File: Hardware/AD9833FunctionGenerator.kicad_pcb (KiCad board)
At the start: 4 copper layers, 50.8 x 128.3 mm, 37 parts, among them U1 LM7805_TO220

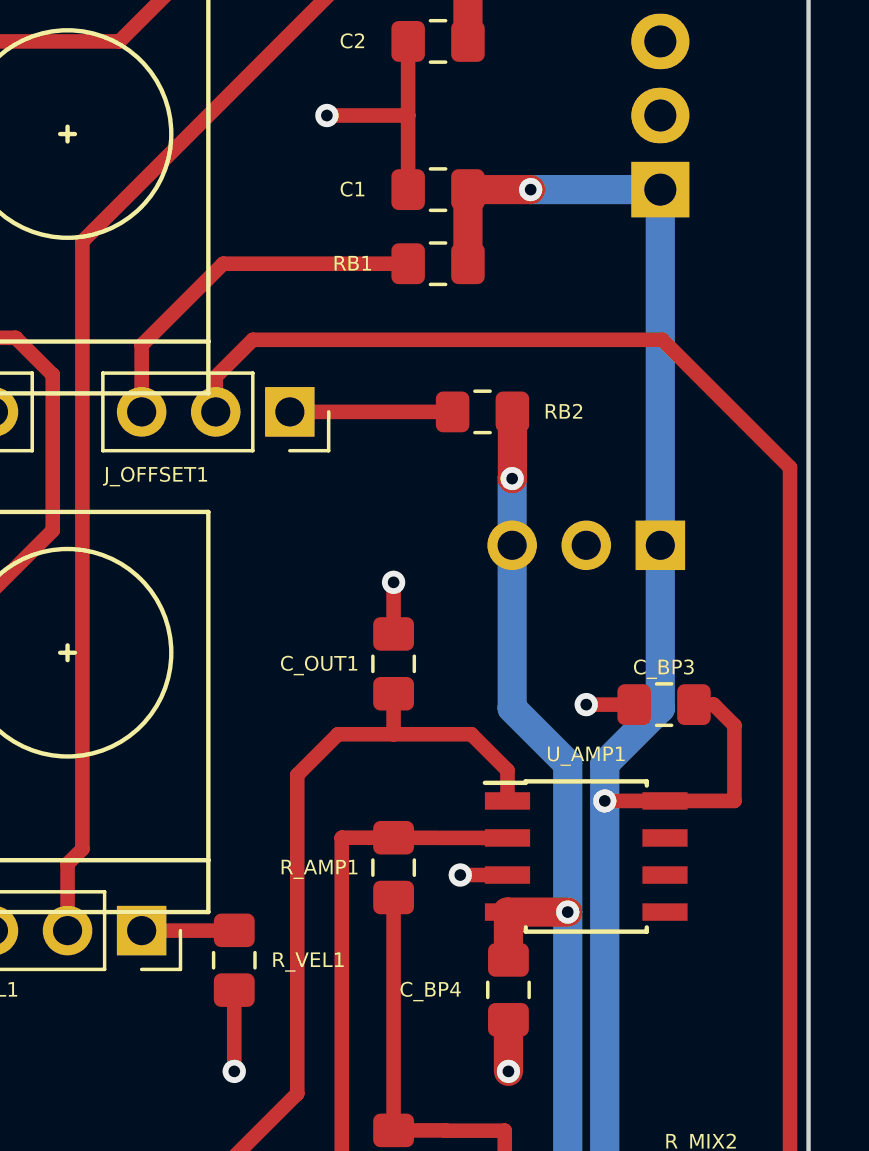
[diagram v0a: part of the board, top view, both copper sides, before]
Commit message: Changed J_PWR1 from 01x03 to 02x05
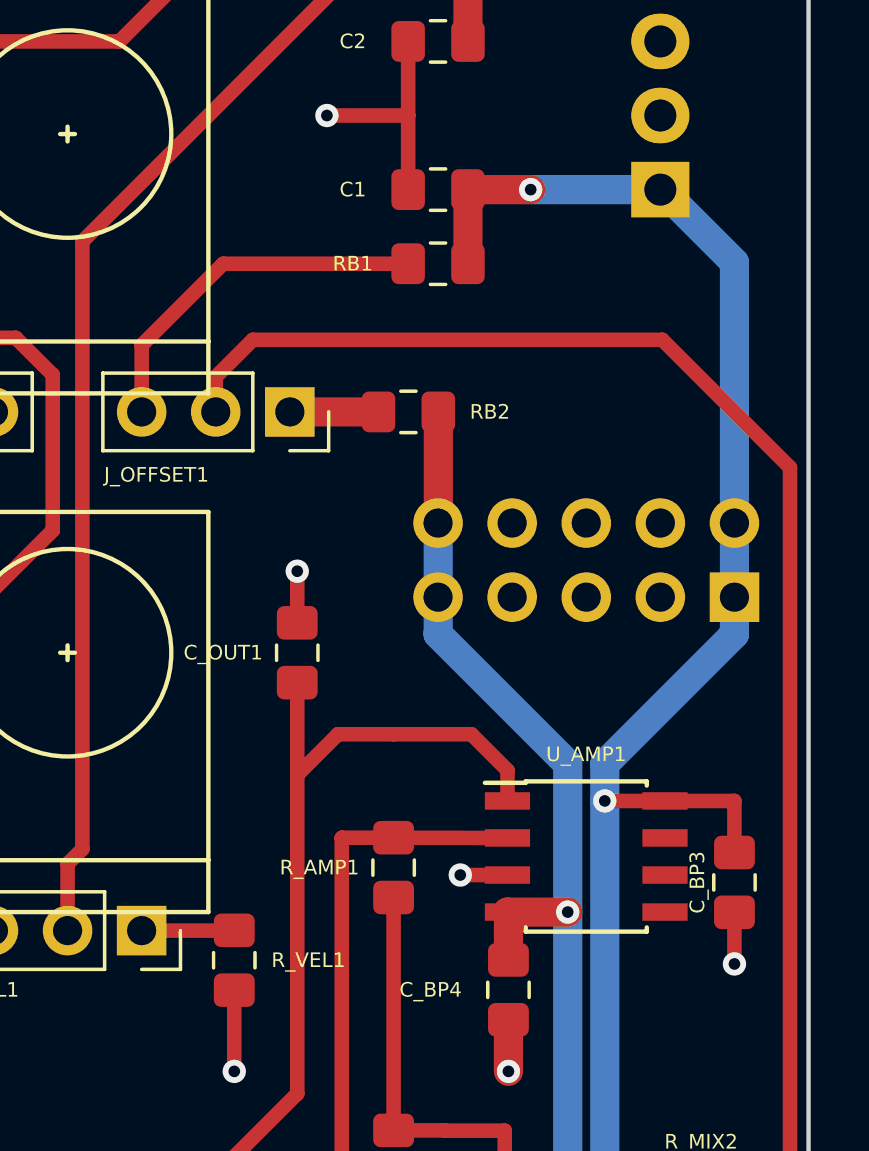
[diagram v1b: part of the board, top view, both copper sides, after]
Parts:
- J_PWR1: value Conn_01x03 -> Conn_02x05_Odd_Even; footprint Connector_PinSocket_2.54mm:PinSocket_1x03_P2.54mm_Vertical -> Connector_PinHeader_2.54mm:PinHeader_2x05_P2.54mm_Vertical
- moved C_BP3 6.56 mm to (99.1, 120.3), turned to 270 degrees
- moved C_OUT1 3.32 mm to (84.1, 112.4)
- moved J_PWR1 3.10 mm to (99.1, 110.5)
- moved RB2 2.54 mm to (87.9, 104.1)
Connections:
- J_PWR1 pad 2: /GND -> /+12V
- J_PWR1 pad 3: /-12V -> /GND
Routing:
- net Net-(J_OFFSET1-Pad1): track 5.58 -> 3.04 mm
- net Net-(C_OUT1-Pad1): track 145.1 -> 146.8 mm
- net /-12V: track 49.8 -> 50.8 mm, vias 3 -> 2
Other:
- board text added: "+12V"
- board text added: "-12V"
- board text added: "| —-— GND —-— |"

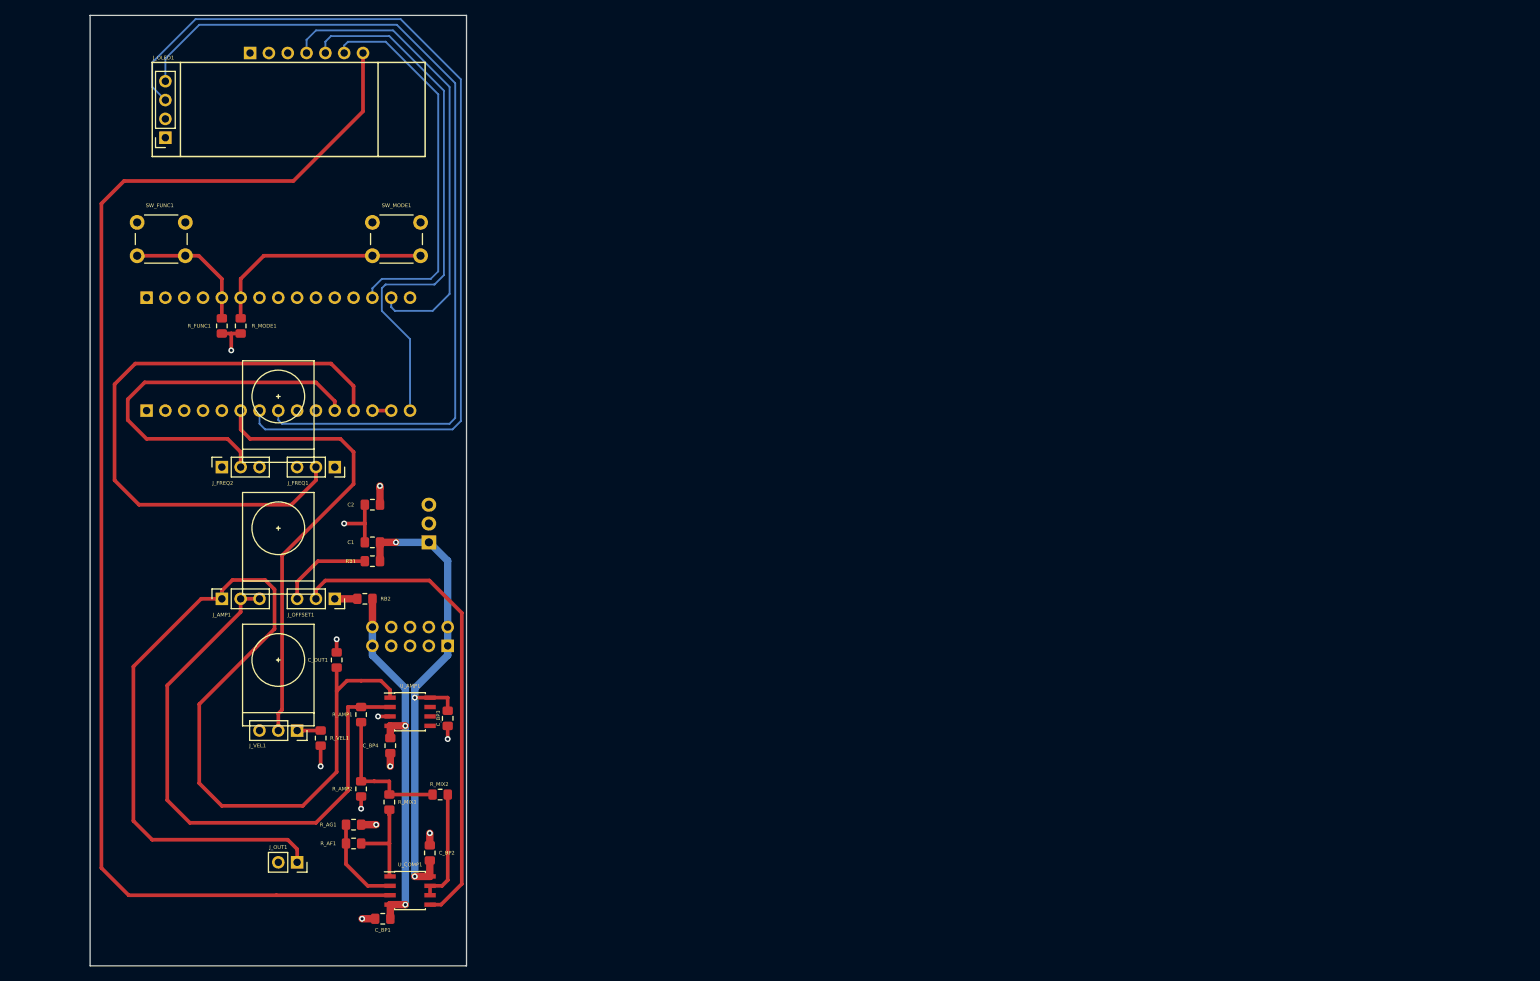
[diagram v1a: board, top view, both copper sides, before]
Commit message: Created board layout RevB. Right-angled to front panel, with front facing aux board(OLED/Buttons)
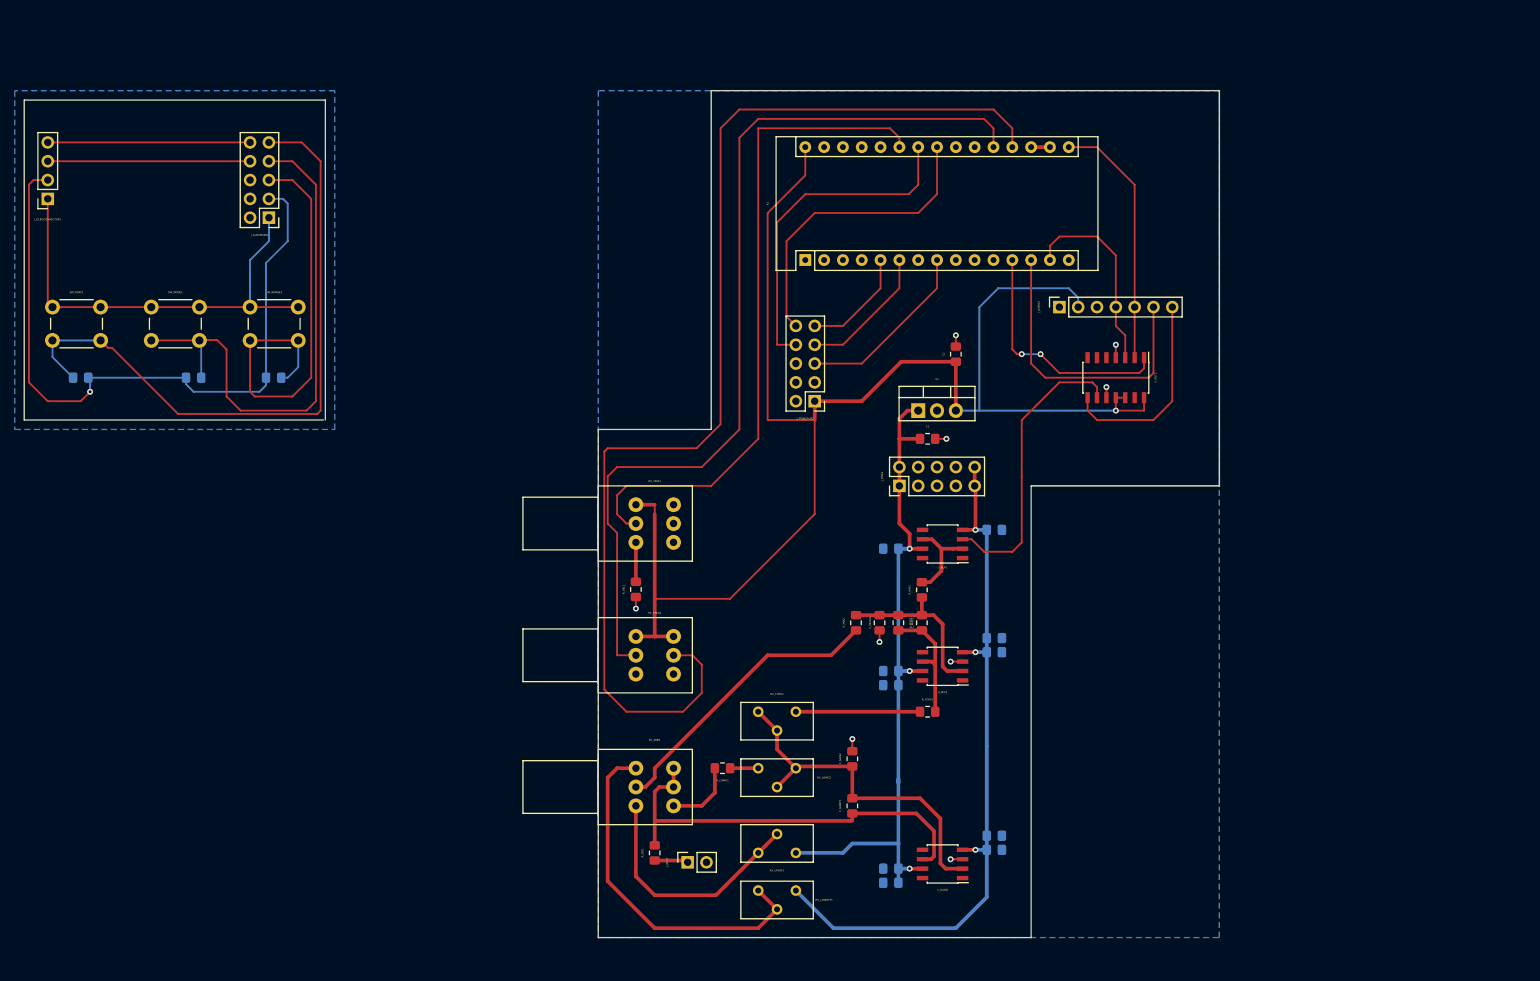
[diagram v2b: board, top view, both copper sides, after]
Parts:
- removed C_BP1, C_BP2, C_BP3, C_BP4: 100nF, Capacitor_SMD:C_0805_2012Metric_Pad1.15x1.40mm_HandSolder
- removed C_OUT1: 10nF, Capacitor_SMD:C_0805_2012Metric_Pad1.15x1.40mm_HandSolder
- removed J_AMP1, J_FREQ1, J_FREQ2, J_OFFSET1, J_VEL1: Conn_01x03, Connector_PinSocket_2.54mm:PinSocket_1x03_P2.54mm_Vertical
- removed J_OLED1: Conn_01x04, Connector_PinSocket_2.54mm:PinSocket_1x04_P2.54mm_Vertical
- removed J_TX1, J_VIN1: Conn_01x15, Connector_PinSocket_2.54mm:PinSocket_1x15_P2.54mm_Vertical
- removed RB1: 8K2, Resistor_SMD:R_0805_2012Metric_Pad1.15x1.40mm_HandSolder
- removed RB2: 1K, Resistor_SMD:R_0805_2012Metric_Pad1.15x1.40mm_HandSolder
- removed REF** (x3): PTH901_Outline, PTH901:PTH901_Outline
- removed R_AF1: 15K, Resistor_SMD:R_0805_2012Metric_Pad1.15x1.40mm_HandSolder
- removed R_AG1: 1K2, Resistor_SMD:R_0805_2012Metric_Pad1.15x1.40mm_HandSolder
- removed R_AMP1: 1K5, Resistor_SMD:R_0805_2012Metric_Pad1.15x1.40mm_HandSolder
- removed R_AMP2: 470R, Resistor_SMD:R_0805_2012Metric_Pad1.15x1.40mm_HandSolder
- removed U_AMP1, U_COMP1: TL072, Package_SO:SOIC-8_3.9x4.9mm_P1.27mm
- added A1: Arduino_Nano_v3.x, Module:Arduino_Nano, F.Cu at (147.3, 58.4)
- added C_BUFBP1: 100nF, Capacitor_SMD:C_0805_2012Metric_Pad1.15x1.40mm_HandSolder, B.Cu at (158.9, 97.4)
- added C_BUFBP2: 100nF, Capacitor_SMD:C_0805_2012Metric_Pad1.15x1.40mm_HandSolder, B.Cu at (172.8, 94.8)
- added C_GAIN2: 470pF, Capacitor_SMD:C_0805_2012Metric_Pad1.15x1.40mm_HandSolder, F.Cu at (153.7, 125.7)
- added C_GAINBP1: 10nF, Capacitor_SMD:C_0805_2012Metric_Pad1.15x1.40mm_HandSolder, B.Cu at (158.9, 140.6)
- added C_GAINBP2: 2.2uF TANT., Capacitor_SMD:C_0805_2012Metric_Pad1.15x1.40mm_HandSolder, B.Cu at (158.9, 142.5)
- added C_GAINBP3: 10nF, Capacitor_SMD:C_0805_2012Metric_Pad1.15x1.40mm_HandSolder, B.Cu at (172.8, 136.1)
- added C_GAINBP4: 2.2uF TANT., Capacitor_SMD:C_0805_2012Metric_Pad1.15x1.40mm_HandSolder, B.Cu at (172.8, 138.0)
- added C_GAINF1: ?, Capacitor_SMD:C_0805_2012Metric_Pad1.15x1.40mm_HandSolder, F.Cu at (153.7, 132.1)
- added C_MIXBP1: 10nF, Capacitor_SMD:C_0805_2012Metric_Pad1.15x1.40mm_HandSolder, B.Cu at (158.9, 113.9)
- added C_MIXBP2: 2.2uF TANT., Capacitor_SMD:C_0805_2012Metric_Pad1.15x1.40mm_HandSolder, B.Cu at (158.9, 115.8)
- added C_MIXBP3: 10nF, Capacitor_SMD:C_0805_2012Metric_Pad1.15x1.40mm_HandSolder, B.Cu at (172.8, 109.4)
- added C_MIXBP4: 2.2pF TANT., Capacitor_SMD:C_0805_2012Metric_Pad1.15x1.40mm_HandSolder, B.Cu at (172.8, 111.3)
- added C_MIXF1: ?, Capacitor_SMD:C_0805_2012Metric_Pad1.15x1.40mm_HandSolder, F.Cu at (163.1, 107.4)
- added C_MIXIN1: ?, Capacitor_SMD:C_0805_2012Metric_Pad1.15x1.40mm_HandSolder, F.Cu at (157.3, 107.4)
- added J_AUX2MAIN2: Conn_02x05_Odd_Even, Connector_PinHeader_2.54mm:PinHeader_2x05_P2.54mm_Vertical, F.Cu at (74.9, 52.7)
- added J_MAIN2AUX1: Conn_02x05_Odd_Even, Connector_PinHeader_2.54mm:PinHeader_2x05_P2.54mm_Vertical, F.Cu at (148.6, 77.5)
- added J_OLEDCONNECTOR1: Conn_01x04, Connector_PinSocket_2.54mm:PinSocket_1x04_P2.54mm_Vertical, F.Cu at (45.1, 50.2)
- added RV_AMP1: B10K, PTH901:PTH901, F.Cu at (127.0, 129.5)
- added RV_FREQ1: B10K, PTH901:PTH901, F.Cu at (127.0, 111.8)
- added RV_LOWG1: 100R, Potentiometer_THT:Potentiometer_Bourns_3296Y_Vertical, F.Cu at (146.1, 127.0)
- added RV_LOWOFF1: 100K, Potentiometer_THT:Potentiometer_Bourns_3296Y_Vertical, F.Cu at (146.1, 143.5)
- added RV_TIME1: B10K, PTH901:PTH901, F.Cu at (127.0, 94.0)
- added RV_TOPG1: 10K, Potentiometer_THT:Potentiometer_Bourns_3296Y_Vertical, F.Cu at (146.1, 119.4)
- added RV_UPOFF1: 100K, Potentiometer_THT:Potentiometer_Bourns_3296Y_Vertical, F.Cu at (141.0, 138.4)
- added R_ISO1: 600R 1%, Resistor_SMD:R_0805_2012Metric_Pad1.15x1.40mm_HandSolder, F.Cu at (127.0, 138.4)
- added R_LOWG1: 120R, Resistor_SMD:R_0805_2012Metric_Pad1.15x1.40mm_HandSolder, F.Cu at (136.1, 127.0)
- added R_MIXF1: 10K, Resistor_SMD:R_0805_2012Metric_Pad1.15x1.40mm_HandSolder, F.Cu at (159.9, 107.4)
- added R_RANGE1: 1K, Resistor_SMD:R_0805_2012Metric_Pad1.15x1.40mm_HandSolder, B.Cu at (75.6, 74.3)
- added R_TOPG1: 330R, Resistor_SMD:R_0805_2012Metric_Pad1.15x1.40mm_HandSolder, F.Cu at (163.8, 119.4)
- added SW_RANGE1: SW_SPST, Button_Switch_THT:SW_PUSH_6mm, F.Cu at (72.4, 64.8)
- added U_BUF1: TL071, Package_SO:SOIC-8_3.9x4.9mm_P1.27mm, F.Cu at (165.8, 96.7)
- added U_GAIN1: LM7171, Package_SO:SOIC-8_3.9x4.9mm_P1.27mm, F.Cu at (165.8, 139.9)
- added U_MIX1: LM7171, Package_SO:SOIC-8_3.9x4.9mm_P1.27mm, F.Cu at (165.8, 113.3)
- added U_POT1: MCP42050, Package_SO:SOIC-14_3.9x8.7mm_P1.27mm, F.Cu at (189.2, 74.3)
- J_AD9833, J_PWR1, U1: moved to F.Cu
- R_FUNC1, R_MODE1: moved to B.Cu
- R_MIX1, R_MIX2: value 1K -> 10K
- R_VEL1: value 1K -> 100R
- moved J_AD9833 114.5 mm to (181.6, 64.8), turned to 90 degrees
- moved C2 81.3 mm to (167.6, 71.1), turned to 90 degrees
- moved R_MIX1 77.4 mm to (163.1, 102.9)
- moved C1 76.2 mm to (163.8, 82.5), turned to 0 degrees
- moved U1 68.4 mm to (162.6, 78.7), turned to 0 degrees
- moved J_PWR1 64.7 mm to (160.0, 88.9)
- moved R_MIX2 60.7 mm to (154.2, 107.4), turned to 90 degrees
- moved J_OUT1 52.7 mm to (131.4, 139.7), turned to 90 degrees
- moved R_VEL1 47.0 mm to (124.5, 102.9)
- moved SW_MODE1 32.0 mm to (59.1, 64.8)
- moved R_FUNC1 20.3 mm to (49.5, 74.3), turned to 180 degrees
- moved SW_FUNC1 16.2 mm to (45.7, 64.8)
- moved R_MODE1 9.44 mm to (64.8, 74.3), turned to 0 degrees
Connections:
- net /FUNC1 renamed /AuxiliaryBoard/WAVEBTN_AUX
- net /MODE1 renamed /AuxiliaryBoard/MODEBTN_AUX
- J_AD9833 pad 7: /SIGFUNC -> /FUNCSIG
- R_FUNC1 pad 1: /GND -> /AuxiliaryBoard/GND_AUX
- R_MIX1 pad 1: Net-(R_AF1-Pad1) -> Net-(C_MIXF1-Pad2)
- R_MIX1 pad 2: Net-(R_AMP1-Pad2) -> Net-(R_MIX1-Pad2)
- R_MIX2 pad 2: Net-(R_AMP1-Pad2) -> Net-(C_MIXF1-Pad2)
- R_MODE1 pad 1: /GND -> /AuxiliaryBoard/GND_AUX
- SW_FUNC1 pad 1: /5V -> /AuxiliaryBoard/5V_AUX
- SW_MODE1 pad 1: /5V -> /AuxiliaryBoard/5V_AUX
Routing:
- net /5V: track 2.54 -> 200.4 mm
- net /SIGFUNC: track 179.1 -> 0.00 mm
- net Net-(J_OUT1-Pad1): track 146.8 -> 4.55 mm
- net /AuxiliaryBoard/GND_AUX: track 0.00 -> 95.5 mm, vias 0 -> 1
- net /SCL: track 129.5 -> 45.3 mm
- net Net-(J_AMP1-Pad2): track 78.2 -> 0.00 mm
- net /SDA: track 118.2 -> 41.3 mm
- net /FREQ1: track 82.6 -> 156.9 mm
- net /FREQ2: track 53.1 -> 125.4 mm
- net /AuxiliaryBoard/WAVEBTN_AUX: track 18.0 -> 88.4 mm
- net Net-(J_OFFSET1-Pad2): track 65.2 -> 0.00 mm
- net /AuxiliaryBoard/5V_AUX: track 0.00 -> 61.2 mm
- net /AuxiliaryBoard/RANGEBTN_AUX: track 0.00 -> 60.4 mm
- net Net-(C_GAINF1-Pad1): track 0.00 -> 57.4 mm
- net Net-(RV_AMP1-Pad3): track 0.00 -> 48.4 mm
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- added copper zone on B.Cu, net /AuxiliaryBoard/GND_AUX
- added copper zone on B.Cu, net /GND
- removed copper zone on In1.Cu, net /5V
- removed copper zone on In2.Cu, net /GND
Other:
- board size 50.8 x 128.3 mm -> 161.3 x 114.3 mm
- copper layers 4 -> 2
- board text removed: "+12V"
- board text removed: "-12V"
- board text removed: "| —-— GND —-— |"

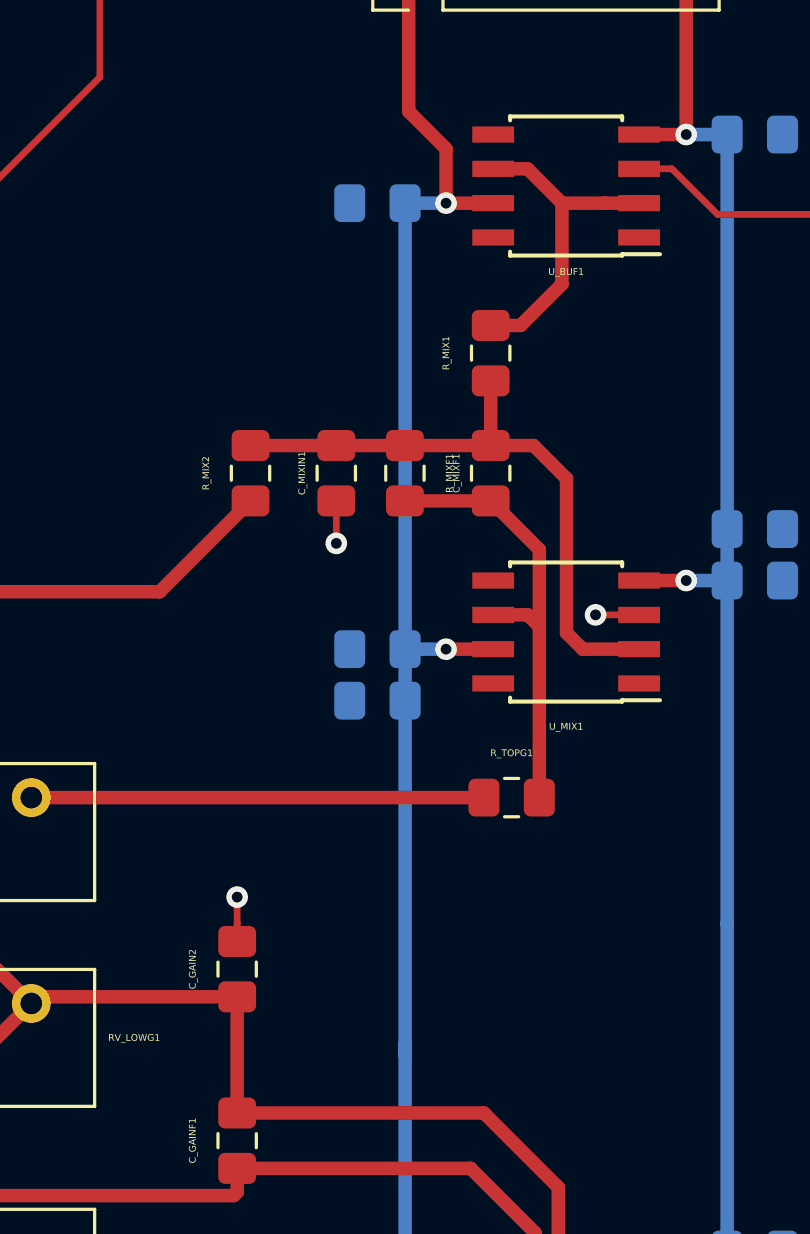
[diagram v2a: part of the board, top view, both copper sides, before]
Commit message: Tidied up schematic. Added sub-sheets
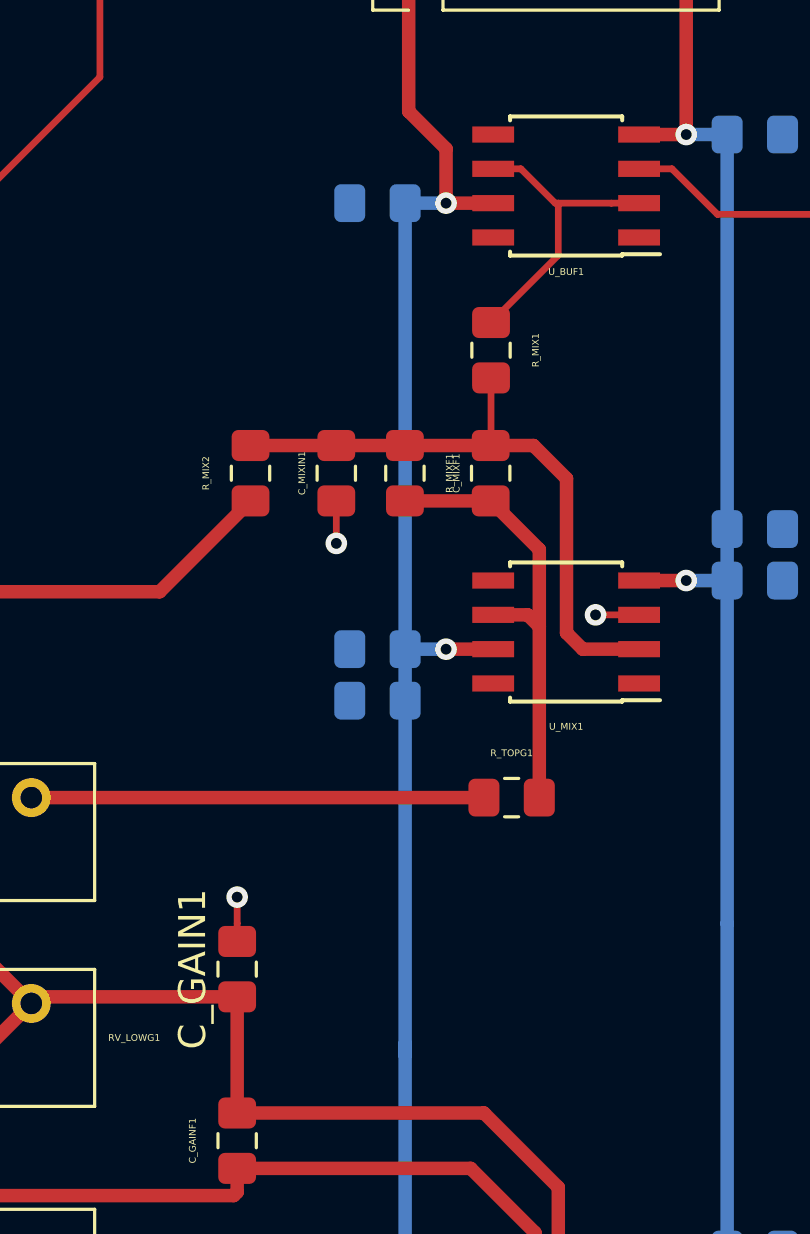
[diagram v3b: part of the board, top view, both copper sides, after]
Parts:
- removed C_GAIN2: 470pF, Capacitor_SMD:C_0805_2012Metric_Pad1.15x1.40mm_HandSolder
- added C_GAIN1: 470pF, Capacitor_SMD:C_0805_2012Metric_Pad1.15x1.40mm_HandSolder, F.Cu at (153.7, 125.7)
- C_GAINBP1, C_MIXBP1: value 10nF -> 2.2uF TANT.
- C_GAINBP2, C_MIXBP2: value 2.2uF TANT. -> 10nF
- moved R_MIX1 0.11 mm to (163.1, 102.8), turned to 270 degrees
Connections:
- net /DDSOUT renamed /DDS_REDUX
- net /FUNCSIG renamed /DDS_SIG
- net Net-(J_OUT1-Pad1) renamed /OutputSection/SIGOUT
- R_MIX1 pad 1: Net-(C_MIXF1-Pad2) -> Net-(R_MIX1-Pad1)
- R_MIX1 pad 2: Net-(R_MIX1-Pad2) -> Net-(C_MIXF1-Pad2)
- U_BUF1 pad 2: Net-(R_MIX1-Pad2) -> Net-(R_MIX1-Pad1)
- U_BUF1 pad 6: Net-(R_MIX1-Pad2) -> Net-(R_MIX1-Pad1)
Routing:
- net Net-(R_MIX1-Pad2): track 12.2 -> 0.00 mm
- net Net-(R_MIX1-Pad1): track 0.00 -> 11.4 mm
